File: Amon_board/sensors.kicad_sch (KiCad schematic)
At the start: 39 parts, among them J10 GTFP08131Y2HR, J11 Conn_01x03_Male, J12 Conn_01x06_Male, J13 Conn_01x04_Male, J14 Conn_01x04_Male, J15 Conn_01x06_Male, J16 Conn_02x09_Odd_Even, J6 Conn_02x04_Odd_Even, J7 Red leds, J8 White leds, J9 Conn_02x04_Odd_Even, M1 Servo_X+, M2 Servo_X-, M3 Servo_Y+, M4 Servo_Y-, Q1 BC817, Q2 BC817, U6 MPU-6050, U7 BME280

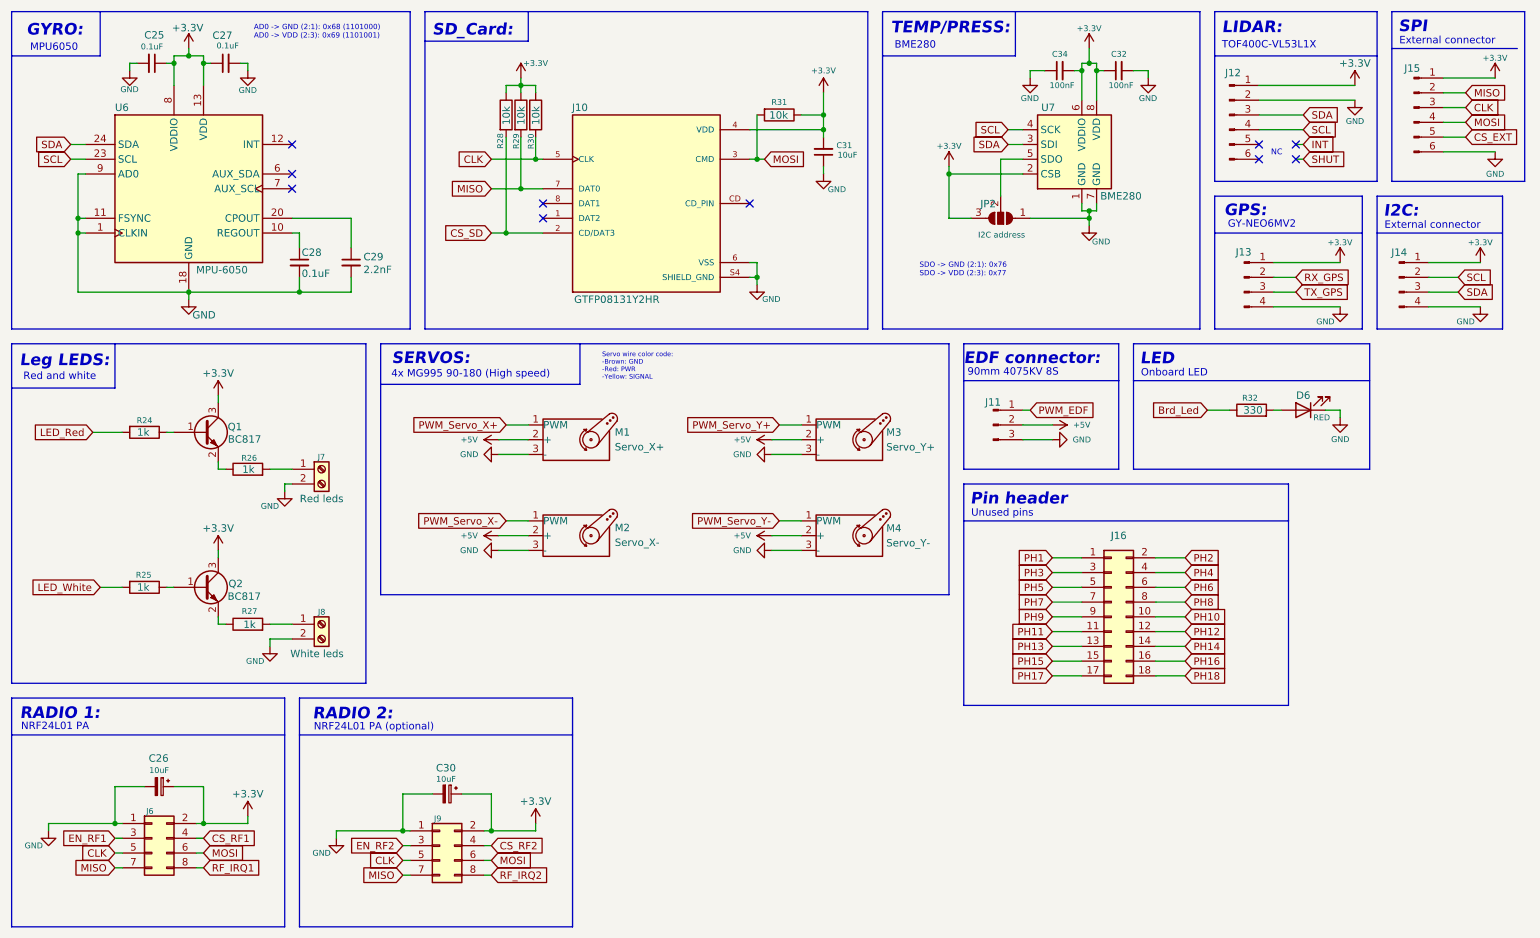
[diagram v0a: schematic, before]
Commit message: PCB update, stl update (pcb holder)
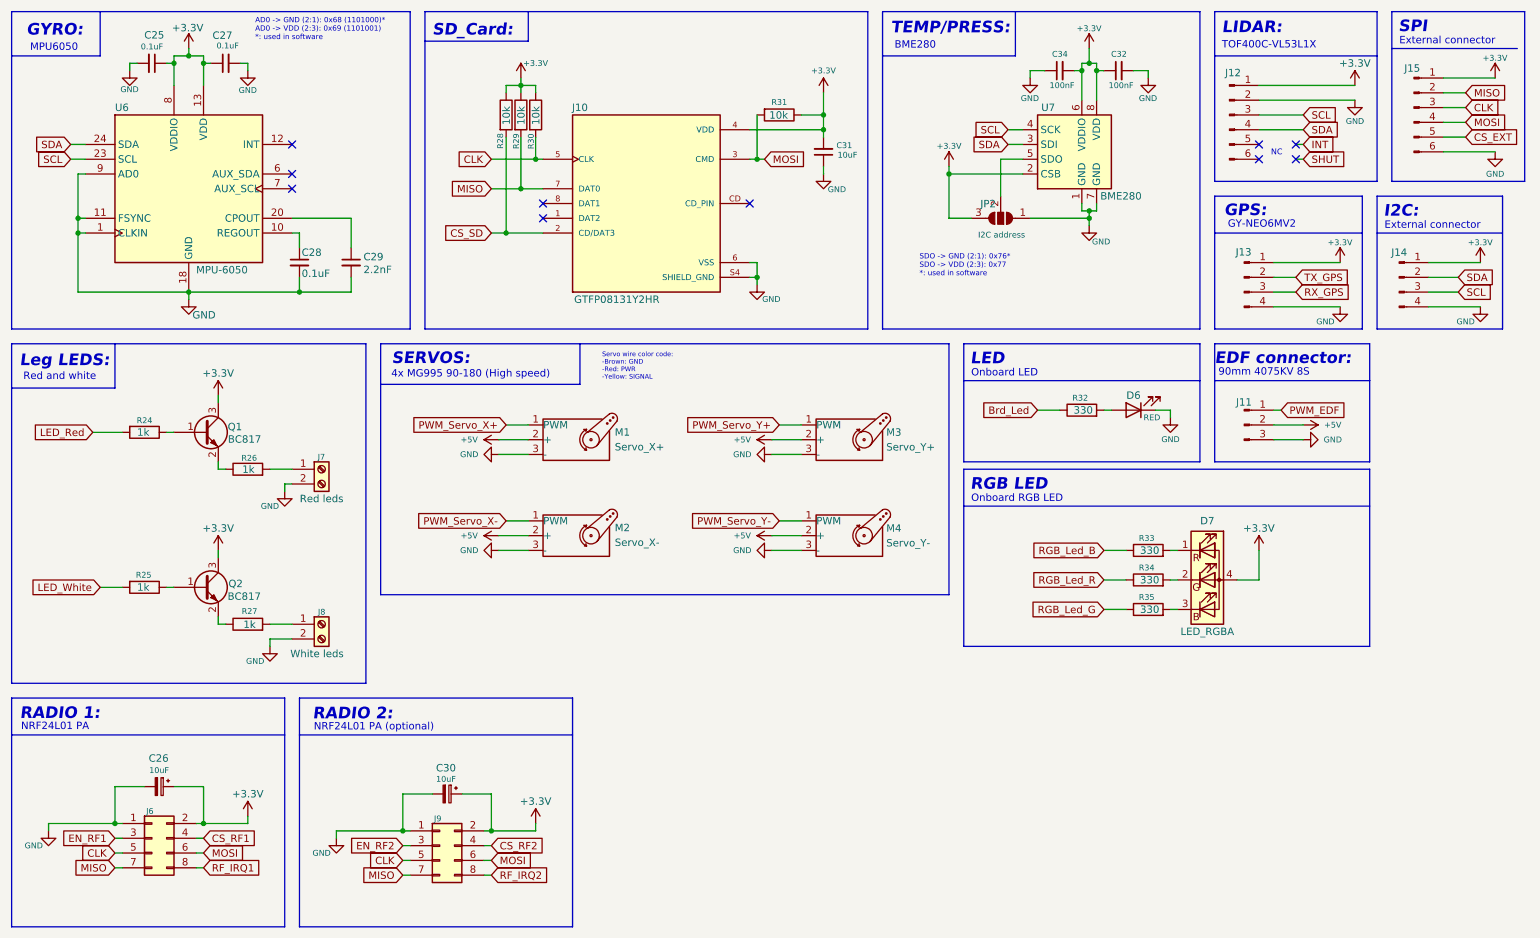
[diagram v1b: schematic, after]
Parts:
- removed J16: Conn_02x09_Odd_Even, Connector_PinHeader_1.27mm:PinHeader_2x09_P1.27mm_Vertical, symbol Connector_Generic:Conn_02x09_Odd_Even
- added D7: LED_RGBA, LED_SMD:LED_Cree-PLCC4_3.2x2.8mm_CCW, symbol Device:LED_RGBA
- added R33, R34, R35: 330, Resistor_SMD:R_0603_1608Metric, symbol Device:R
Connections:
- net +3V3: now also D7.4 (A)
- net RX_GPS: now also J13.3 (Pin_3); no longer J13.2 (Pin_2)
- net SCL: now also J12.3 (Pin_3), J14.3 (Pin_3); no longer J12.4 (Pin_4), J14.2 (Pin_2)
- net SDA: now also J12.4 (Pin_4), J14.2 (Pin_2); no longer J12.3 (Pin_3), J14.3 (Pin_3)
- net TX_GPS: now also J13.2 (Pin_2); no longer J13.3 (Pin_3)
- new net: D7.3 (BK), R35.2
- new net: D7.1 (RK), R33.2
- new net: D7.2 (GK), R34.2
- new net RGB_Led_B: R33.1
- new net RGB_Led_G: R35.1
- new net RGB_Led_R: R34.1
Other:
- note added: "AD0 -> GND (2:1): 0x68 (1101000)* AD0 -> VDD (2:3): 0x69 (1101001) *: used in software"
- note added: "Onboard RGB LED"
- note added: "RGB LED"
- note added: "SDO -> GND (2:1): 0x76* SDO -> VDD (2:3): 0x77 *: used in software"
- note removed: "AD0 -> GND (2:1): 0x68 (1101000) AD0 -> VDD (2:3): 0x69 (1101001)"
- note removed: "Pin header"
- note removed: "SDO -> GND (2:1): 0x76 SDO -> VDD (2:3): 0x77"
- note removed: "Unused pins"
- moved on the sheet: D6, J11, R32
